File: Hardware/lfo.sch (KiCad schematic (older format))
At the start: 52 parts, among them Q5 2N3904, Q6 2N3904, Q7 2N3904, Q8 2N3904

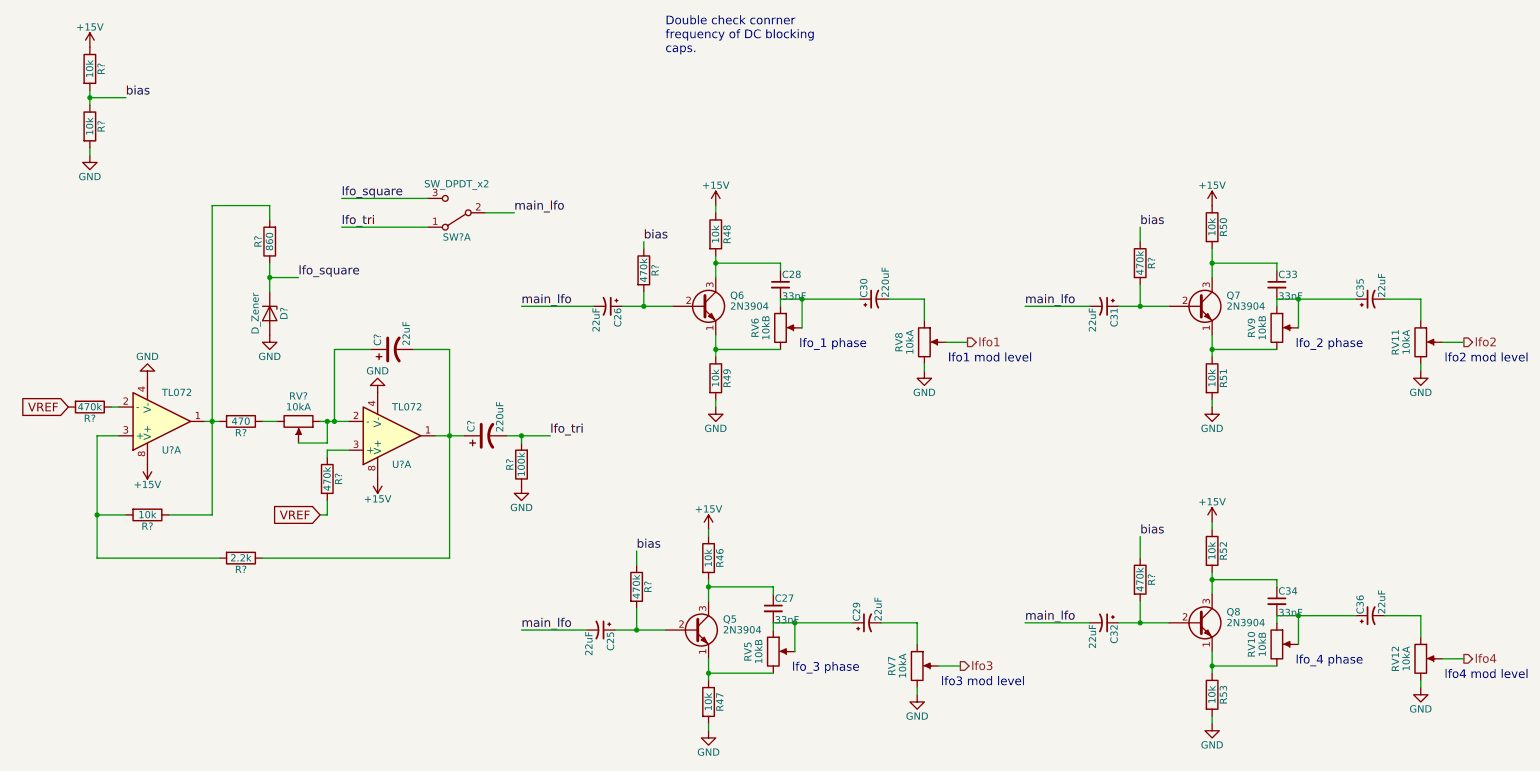
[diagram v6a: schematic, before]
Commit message: associate footprints with all components
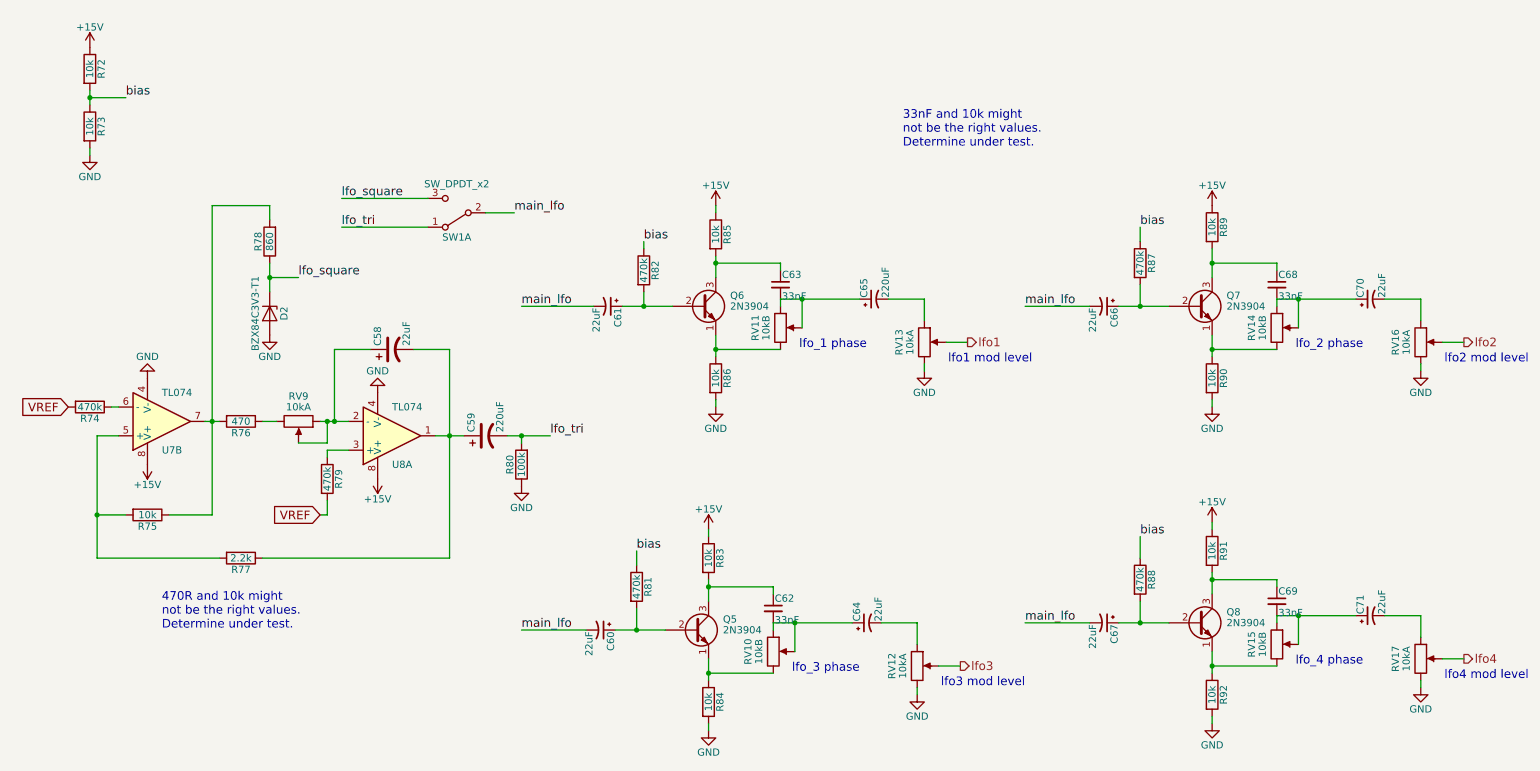
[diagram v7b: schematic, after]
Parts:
- C58: renamed from C?; footprint (none) -> Capacitors_SMD:CP_Elec_5x5.7
- C59: renamed from C?; footprint (none) -> Capacitors_SMD:CP_Elec_8x10
- C60: renamed from C25; footprint (none) -> Capacitors_SMD:CP_Elec_5x5.7
- C61: renamed from C26; footprint (none) -> Capacitors_SMD:CP_Elec_5x5.7
- C62: renamed from C27; footprint (none) -> digikey-footprints:0805
- C63: renamed from C28; footprint (none) -> digikey-footprints:0805
- C64: renamed from C29; footprint (none) -> Capacitors_SMD:CP_Elec_5x5.7
- C65: renamed from C30; footprint (none) -> Capacitors_SMD:CP_Elec_8x10
- C66: renamed from C31; footprint (none) -> Capacitors_SMD:CP_Elec_5x5.7
- C67: renamed from C32; footprint (none) -> Capacitors_SMD:CP_Elec_5x5.7
- C68: renamed from C33; footprint (none) -> digikey-footprints:0805
- C69: renamed from C34; footprint (none) -> digikey-footprints:0805
- C70: renamed from C35; footprint (none) -> Capacitors_SMD:CP_Elec_5x5.7
- C71: renamed from C36; footprint (none) -> Capacitors_SMD:CP_Elec_5x5.7
- D2: renamed from D?; value D_Zener -> BZX84C3V3-T1; footprint (none) -> digikey-footprints:SOT-23-3
- Q5, Q6, Q7, Q8: footprint TO_SOT_Packages_THT:TO-92_Molded_Narrow -> digikey-footprints:SOT-23-3
- R72, R73, R74, R75, R76, R77, R78, R79, R80, R81, R82, R87, R88: renamed from R?; footprint (none) -> digikey-footprints:0805
- R83: renamed from R46; footprint (none) -> digikey-footprints:0805
- R84: renamed from R47; footprint (none) -> digikey-footprints:0805
- R85: renamed from R48; footprint (none) -> digikey-footprints:0805
- R86: renamed from R49; footprint (none) -> digikey-footprints:0805
- R89: renamed from R50; footprint (none) -> digikey-footprints:0805
- R90: renamed from R51; footprint (none) -> digikey-footprints:0805
- R91: renamed from R52; footprint (none) -> digikey-footprints:0805
- R92: renamed from R53; footprint (none) -> digikey-footprints:0805
- RV10: renamed from RV5; footprint (none) -> Potentiometers:Potentiometer_Bourns_PTV09A-1_Horizontal
- RV11: renamed from RV6; footprint (none) -> Potentiometers:Potentiometer_Bourns_PTV09A-1_Horizontal
- RV12: renamed from RV7; footprint (none) -> Potentiometers:Potentiometer_Bourns_PTV09A-1_Horizontal
- RV13: renamed from RV8; footprint (none) -> Potentiometers:Potentiometer_Bourns_PTV09A-1_Horizontal
- RV14: renamed from RV9; footprint (none) -> Potentiometers:Potentiometer_Bourns_PTV09A-1_Horizontal
- RV15: renamed from RV10; footprint (none) -> Potentiometers:Potentiometer_Bourns_PTV09A-1_Horizontal
- RV16: renamed from RV11; footprint (none) -> Potentiometers:Potentiometer_Bourns_PTV09A-1_Horizontal
- RV17: renamed from RV12; footprint (none) -> Potentiometers:Potentiometer_Bourns_PTV09A-1_Horizontal
- RV9: renamed from RV?; footprint (none) -> Potentiometers:Potentiometer_Bourns_PTV09A-1_Horizontal
- U7: renamed from U?; value TL072 -> TL074; footprint (none) -> digikey-footprints:Humidity_SHT15
- U8: renamed from U?; value TL072 -> TL074; footprint (none) -> digikey-footprints:SMD-5-6_R_3.83x2.79mm
- gave numbers to parts that had none: 1
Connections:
- net at R75.1, R76.2, R78.2: now also U7.7; no longer U7.1
- net at R74.1: now also U7.6 (-); no longer U7.2 (-)
- net at R75.2, R77.2: now also U7.5 (+); no longer U7.3 (+)
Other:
- note added: "33nF and 10k might \nnot be the right values.\nDetermine under test."
- note added: "470R and 10k might \nnot be the right values.\nDetermine under test."
- note removed: "Double check conrner \nfrequency of DC blocking \ncaps."

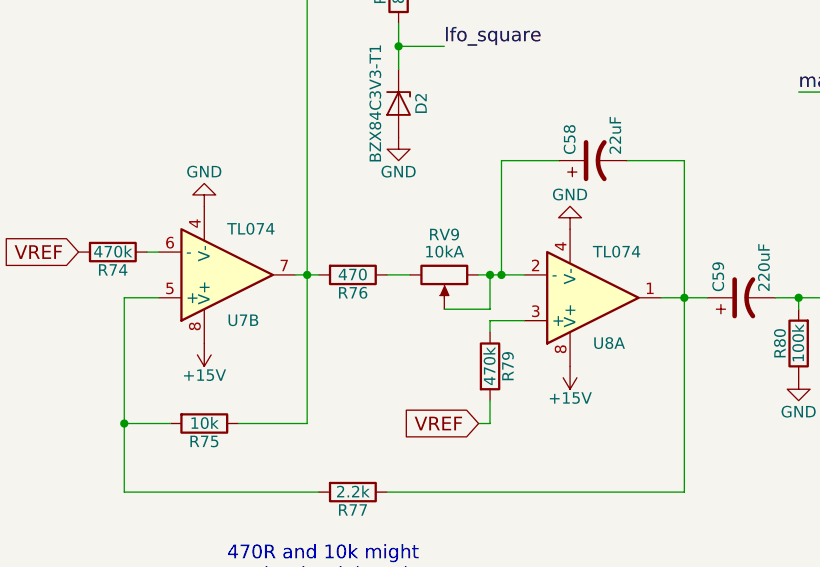
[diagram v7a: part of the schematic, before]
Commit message: fix annotation and footprints for multi-part op amps.
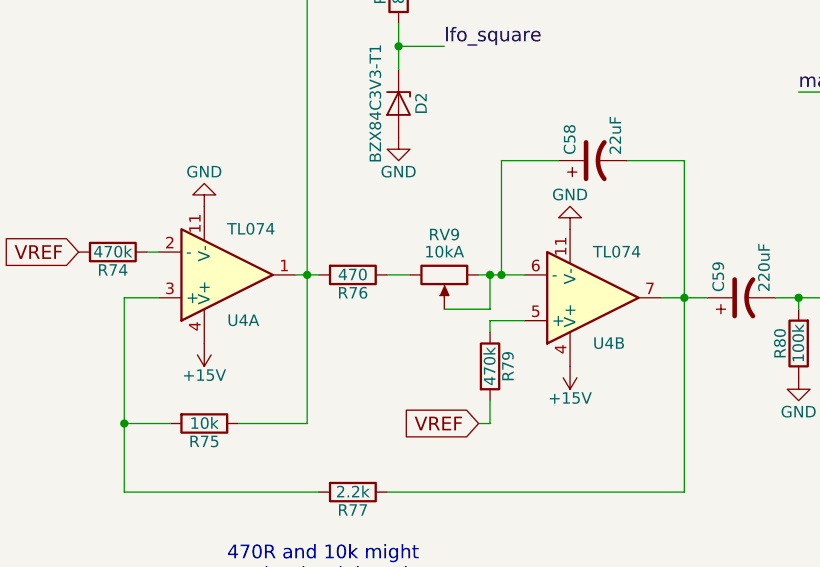
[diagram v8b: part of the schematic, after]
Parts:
- removed U7: TL074, digikey-footprints:Humidity_SHT15, symbol TL072
- removed U8: TL074, digikey-footprints:SMD-5-6_R_3.83x2.79mm, symbol TL072
- added U4: TL074, digikey-footprints:SOIC-14_W3.9mm, symbol TL074
- SW1: footprint (none) -> SparkFun-Electromechanical:SWITCHE-DPDT
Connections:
- net +15V: now also U4.4 (V+), U4.4 (V+)
- net GND: now also U4.11 (V-), U4.11 (V-)
- net at R75.2, R77.2: now also U4.3 (+)
- net at R74.1: now also U4.2 (-)
- net at R75.1, R76.2, R78.2: now also U4.1
- net at C58.2, C59.1, R77.1: now also U4.7
- net at C58.1, RV9.1, RV9.2: now also U4.6 (-)
- net at R79.1: now also U4.5 (+)
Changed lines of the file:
@@
-$EndComp
-$Comp
-L TL072 U7
-U 2 1 5C37EB80
-P 1550 3600
-F 0 "U7" H 1550 3800 50  0000 L CNN
-F 1 "TL074" H 1550 3400 50  0000 L CNN
-F 2 "digikey-footprints:Humidity_SHT15" H 1550 3600 50  0001 C CNN
-F 3 "" H 1550 3600 50  0001 C CNN
-	2    1550 3600
-	1    0    0    1
-$EndComp
-$Comp
-L TL072 U8
-U 1 1 5C37EC7E
-P 3150 3700
-F 0 "U8" H 3150 3900 50  0000 L CNN
-F 1 "TL074" H 3150 3500 50  0000 L CNN
-F 2 "digikey-footprints:SMD-5-6_R_3.83x2.79mm" H 3150 3700 50  0001 C CNN
-F 3 "" H 3150 3700 50  0001 C CNN
-	1    3150 3700
-	1    0    0    1
 $EndComp
 $Comp
@@
 F 0 "SW1" H 3600 2320 50  0000 C CNN
 F 1 "SW_DPDT_x2" H 3600 1950 50  0000 C CNN
-F 2 "" H 3600 2150 50  0001 C CNN
+F 2 "SparkFun-Electromechanical:SWITCHE-DPDT" H 3600 2150 50  0001 C CNN
 F 3 "" H 3600 2150 50  0001 C CNN
 	1    3600 2150
@@
 Text Notes 6700 1700 0    60   ~ 0
 33nF and 10k might \nnot be the right values.\nDetermine under test.
+$Comp
+L TL074 U4
+U 1 1 5C3DFB3A
+P 1550 3600
+F 0 "U4" H 1550 3800 50  0000 L CNN
+F 1 "TL074" H 1550 3400 50  0000 L CNN
+F 2 "digikey-footprints:SOIC-14_W3.9mm" H 1500 3700 50  0001 C CNN
+F 3 "" H 1600 3800 50  0001 C CNN
+	1    1550 3600
+	1    0    0    1
+$EndComp
+$Comp
+L TL074 U4
+U 2 1 5C3E0A6C
+P 3150 3700
+F 0 "U4" H 3150 3900 50  0000 L CNN
+F 1 "TL074" H 3150 3500 50  0000 L CNN
+F 2 "digikey-footprints:SOIC-14_W3.9mm" H 3100 3800 50  0001 C CNN
+F 3 "" H 3200 3900 50  0001 C CNN
+	2    3150 3700
+	1    0    0    1
+$EndComp
 $EndSCHEMATC
